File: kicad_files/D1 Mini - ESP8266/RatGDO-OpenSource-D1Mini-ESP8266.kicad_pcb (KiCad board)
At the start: 2 copper layers, 54.4 x 65.8 mm, 20 parts, among them J1 Screw_Terminal_01x03, J2 Conn_01x10, Q1 2N7002, Q2 AO3400A, Q3 AO3400A, Q4 AO3400A, U1 WeMos_D1_mini

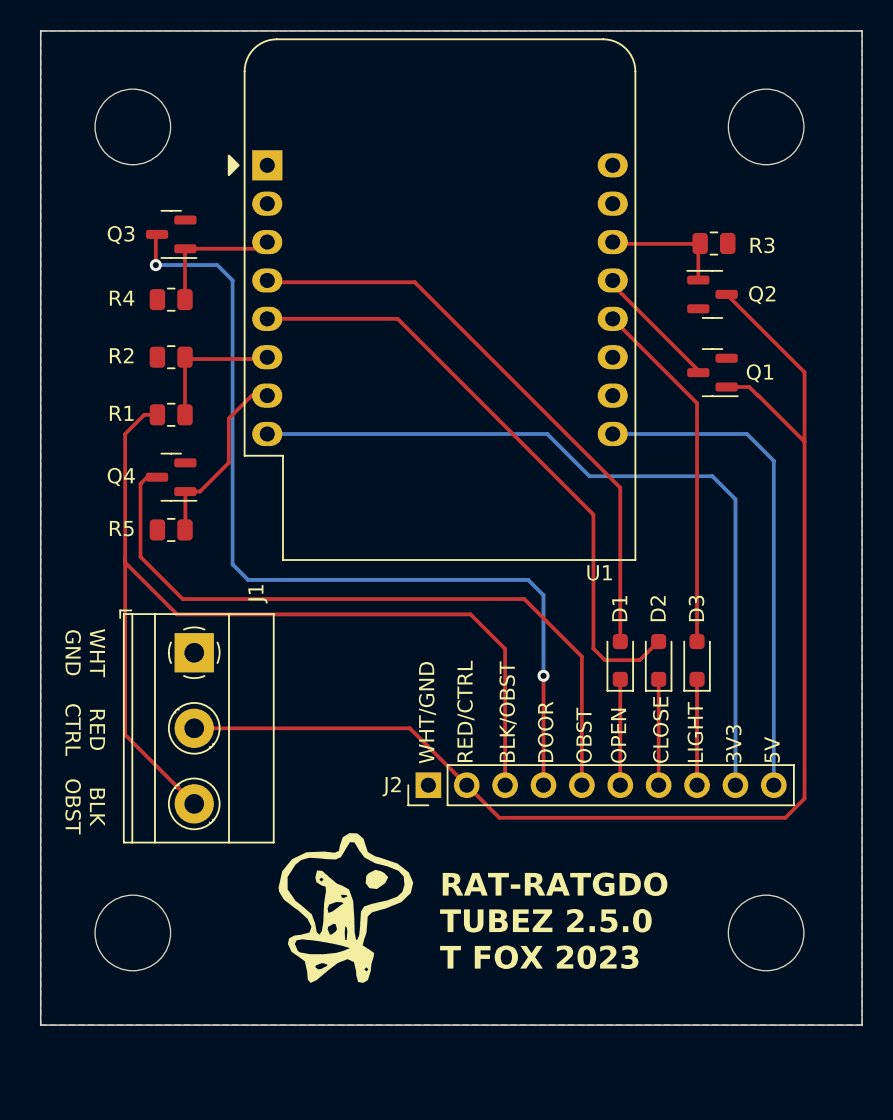
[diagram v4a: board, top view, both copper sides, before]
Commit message: relayout of board
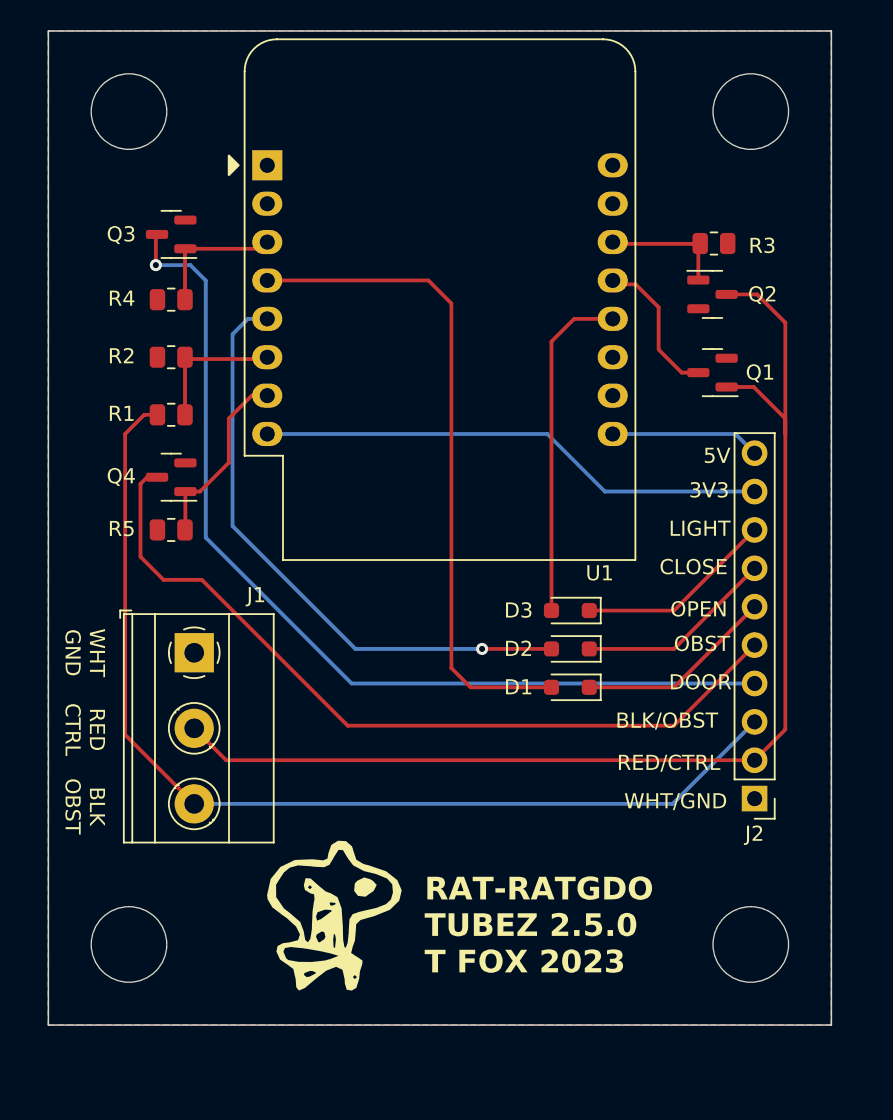
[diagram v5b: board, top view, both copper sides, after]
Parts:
- moved J2 21.6 mm to (161.8, 108.0), turned to 180 degrees
- moved D3 9.01 mm to (149.6, 95.5), turned to 180 degrees
- moved D2 5.89 mm to (149.6, 98.0), turned to 180 degrees
- moved D1 3.75 mm to (149.6, 100.6), turned to 180 degrees
- moved REF** 1.44 mm to (161.5, 62.5)
- moved REF** 1.27 mm to (161.5, 117.6)
- moved REF** 1.05 mm to (120.4, 62.5)
- moved G*** 0.92 mm to (133.9, 115.6)
- moved REF** 0.80 mm to (120.4, 117.6)
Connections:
- net Net-(Q1-D) renamed /ESP_RX
- net Net-(Q2-G) renamed /ESP_TX
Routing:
- net +5V: track 32.9 -> 9.92 mm
- net +3V3: track 51.7 -> 33.8 mm
- net RED/CTRL: track 85.4 -> 78.2 mm
- net STS_OBST: track 46.6 -> 53.6 mm
- net DC_OPEN: track 7.01 -> 13.2 mm
- net DC_LIGHT: track 7.01 -> 13.2 mm
- net DC_CLOSE: track 7.01 -> 13.2 mm
- net Net-(D1-A): track 39.2 -> 44.1 mm
- net STS_DOOR: track 60.0 -> 62.8 mm, vias 2 -> 1
- net BLK/OBST: track 65.9 -> 68.4 mm
- net /ESP_RX: track 8.22 -> 9.84 mm
- net Net-(D3-A): track 23.7 -> 22.5 mm
- net Net-(D2-A): track 41.0 -> 39.9 mm, vias 0 -> 1
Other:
- board size 54.4 x 65.8 mm -> 51.8 x 65.8 mm
- board text added: "A0"
- board text added: "D0"
- board text added: "D1/SCL"
- board text added: "D2/SDA"
- board text added: "D3"
- board text added: "D4"
- board text added: "D5/SCK"
- board text added: "D6/MISO"
- board text added: "D7/MOSI"
- board text added: "D8"
- board text added: "JLCJLCJLCJLC"
- board text added: "RX"
- board text added: "TX"
- board text removed: "5v"
- board text removed: "EN"
- board text removed: "GPIO0"
- board text removed: "GPIO1"
- board text removed: "GPIO12"
- board text removed: "GPIO13"
- board text removed: "GPIO14"
- board text removed: "GPIO15"
- board text removed: "GPIO16"
- board text removed: "GPIO2"
- board text removed: "GPIO3"
- board text removed: "GPIO4"
- board text removed: "GPIO5"
- board text removed: "VCC-3v3"

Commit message: dual connector
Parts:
- removed the REF** at (120.4, 117.6)
- added J3: Screw_Terminal_01x02, TerminalBlock_Phoenix:TerminalBlock_Phoenix_MKDS-1,5-2_1x02_P5.00mm_Horizontal, F.Cu at (124.7, 113.5)
- added REF**: JLCToolingHole_1.152mm, MountingHole:MountingHole_2.1mm, F.Cu at (164.8, 69.1)
- added REF**: JLCToolingHole_1.152mm, MountingHole:MountingHole_2.1mm, F.Cu at (117.1, 69.1)
- added REF**: JLCToolingHole_1.152mm, MountingHole:MountingHole_2.1mm, F.Cu at (142.7, 120.9)
- moved G*** 2.17 mm to (135.9, 116.3)
- moved J1 1.02 mm to (124.7, 97.3)
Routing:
- net +5V: track 9.92 -> 79.2 mm
- net +3V3: track 33.8 -> 96.1 mm
- net BLK/OBST: track 68.4 -> 66.2 mm
- net RED/CTRL: track 78.2 -> 79.0 mm
- net STS_OBST: track 53.6 -> 53.0 mm
